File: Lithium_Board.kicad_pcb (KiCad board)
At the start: 6 copper layers, 80 x 67 mm, 117 parts, among them IC1 BQ25750RRVR, IC2 TPS70933DBVR, IC4 STM32G0B1CBT6N, IC5 TCAN3414DR, IC6 BQ7694204PFBR, J1 XT30PW-M, J2 XT30PW-F, J3 XT30PW-M, J4 S3B-XH-SM4-TB_LF__SN_, J5 TSW-105-07-G-S, J6 Conn_01x06, J7 Conn_01x04, Q1 SIR870ADP-T1-GE3, Q10 MMBT5551LT1G, Q2 SIR870ADP-T1-GE3, Q3 SIR870ADP-T1-GE3, Q4 SIR870ADP-T1-GE3, Q5 SIR870ADP-T1-GE3, Q6 SIR870ADP-T1-GE3, Q7 SIR870ADP-T1-GE3, Q8 SIR870ADP-T1-GE3

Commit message: Small Changes
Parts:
- added C29: 100nF [HV], C0603C104K1RACAUTO:CAPC1608X95N, B.Cu at (117.3, 74.2)
- added C30: 4.7uF [HV], KAM32LR72A475KU:CAPC3225X94N, B.Cu at (114.7, 74.0)
- moved R7 6.59 mm to (157.8, 89.1)
- moved C8 4.88 mm to (164.2, 81.1), turned to 0 degrees
- moved C23 0.88 mm to (174.2, 95.3)
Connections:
- net +48V renamed VIN
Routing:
- net +BATT: track 19.0 -> 7.41 mm, vias 29 -> 27
- net /Q1_D: track 0.00 -> 3.12 mm
- net /Q7_DRAIN: track 1.07 -> 3.84 mm, vias 46 -> 40
- net BQ_SYS: track 2.85 -> 5.42 mm
- net GND: track 65.5 -> 66.5 mm

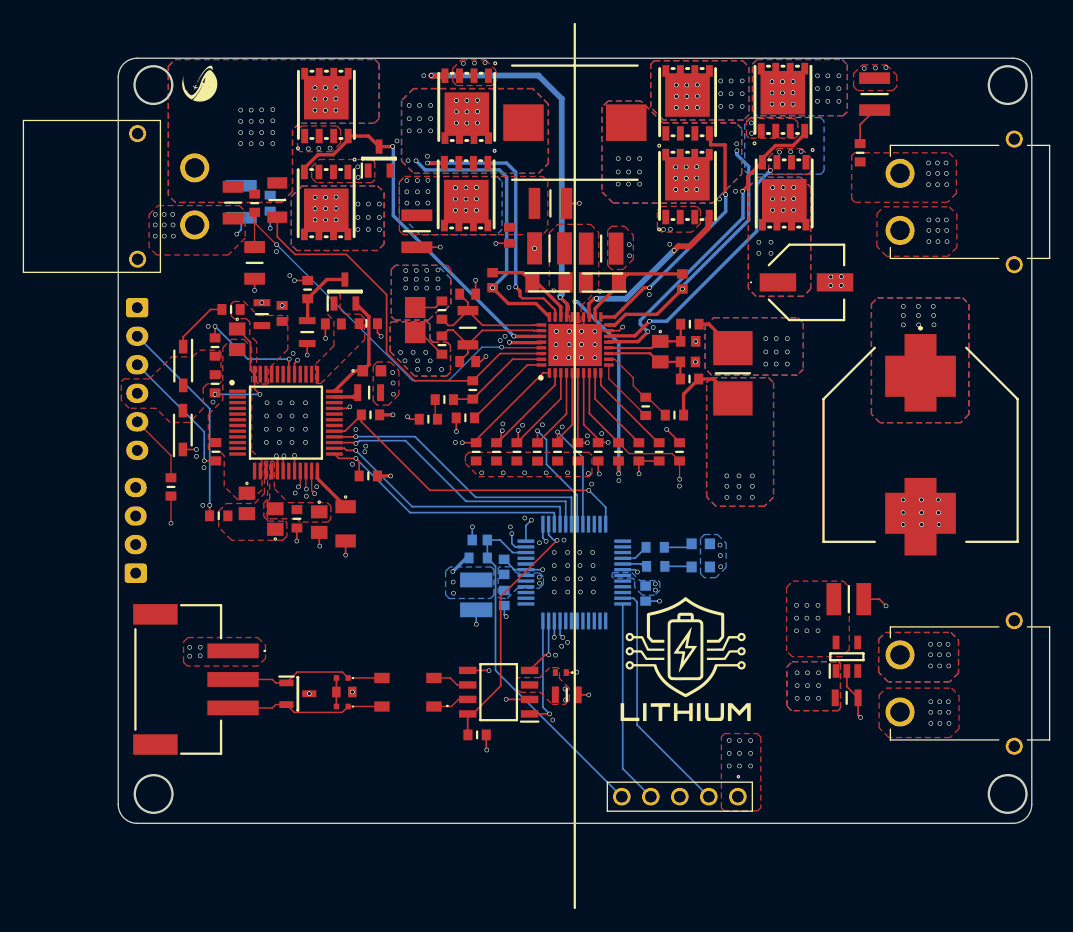
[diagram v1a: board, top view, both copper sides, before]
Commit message: Via Arrays Fixed
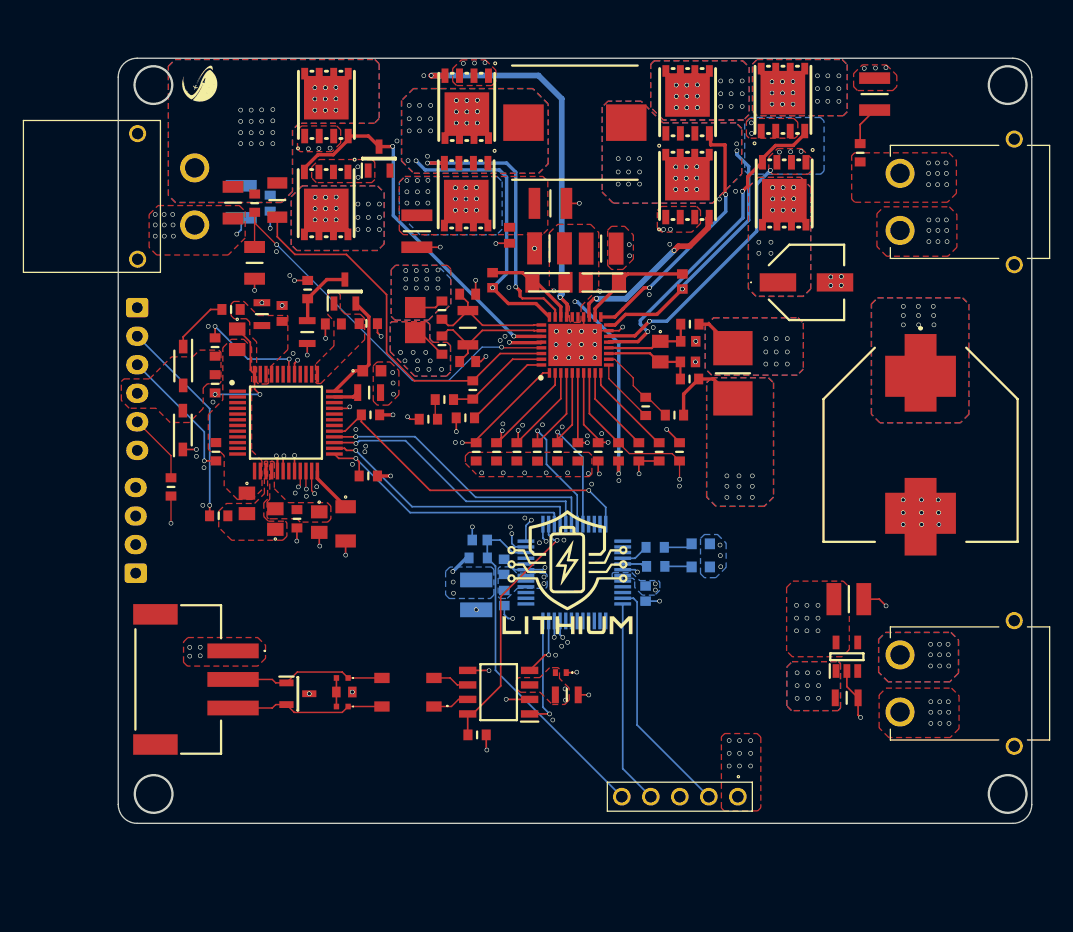
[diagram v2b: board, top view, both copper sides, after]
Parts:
- moved G*** 12.8 mm to (143.3, 106.8)
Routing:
- net GND: track 66.5 -> 66.2 mm, vias 198 -> 166

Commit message: Review Changes #2
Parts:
- moved G*** 1.68 mm to (176.3, 63.9)
- moved G*** 0.99 mm to (112.1, 63.7)
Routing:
- net /SW2: track 22.7 -> 23.5 mm
- net /HIDRV2: track 22.9 -> 22.3 mm
- net /ACDRV: track 33.3 -> 33.8 mm
- net GND: vias 166 -> 168
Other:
- outline, holes or cut-outs redrawn

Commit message: Vias in Pad Fixed
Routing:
- net BQ_SYS: vias 67 -> 76
- net /SW2: vias 20 -> 29
- net /SW1: vias 20 -> 29
- net /Q7_DRAIN: vias 40 -> 49

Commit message: First Big Review Changes
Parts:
- IC2: value TPS70933DBVR -> TPS70933DRVR; footprint TPS70933DBVR:SOT95P280X145-5N -> TPS70933DRVR:SON65P200X200X80-7N
- R11: value 249k -> 249kΩ; footprint RC0603FR-07249KL:RESC1608X55N -> RC0603FR-071KL:RESC1608X55N
- R25: value 34.8k -> 35.2kΩ; footprint RC0603FR-0734K8L:RESC1608X55N -> RC0603FR-071KL:RESC1608X55N
- moved C21 24.5 mm to (145.4, 126.1), turned to -90 degrees
- moved IC2 1.63 mm to (166.1, 113.9), turned to -90 degrees
- turned R11 to 0 degrees
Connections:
- IC2 pad 1: +BATT -> +3V3
- IC2 pad 2: GND -> unconnected-(IC2-NC_1-Pad2)
- IC2 pad 3: unconnected-(IC2-EN-Pad3) -> GND
- IC2 pad 5: +3V3 -> unconnected-(IC2-NC_2-Pad5)
- R11 pad 1: +BATT -> BQ_FB
- R11 pad 2: BQ_FB -> +BATT
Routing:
- net GND: track 66.2 -> 63.3 mm, vias 168 -> 173
- net NRST: track 31.2 -> 30.6 mm
- net +BATT: vias 27 -> 26

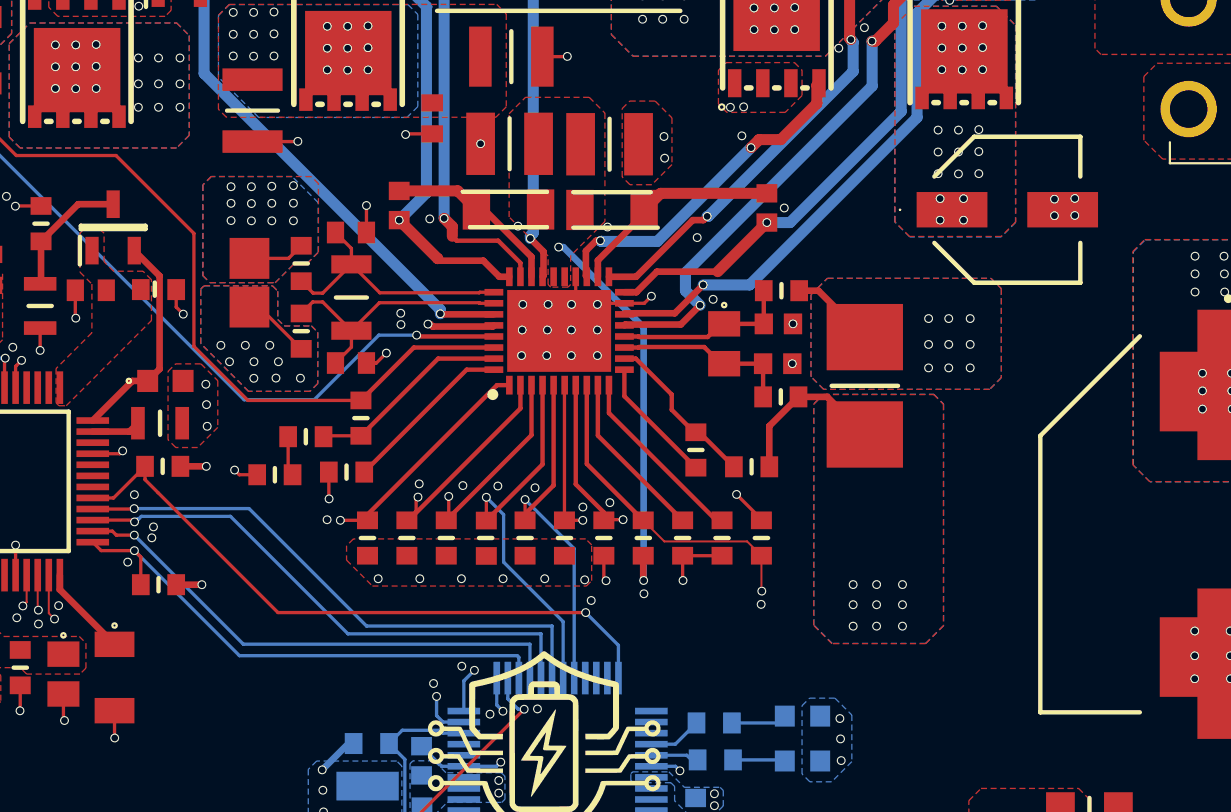
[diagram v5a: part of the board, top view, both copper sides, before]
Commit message: Fixed Big Capacitor
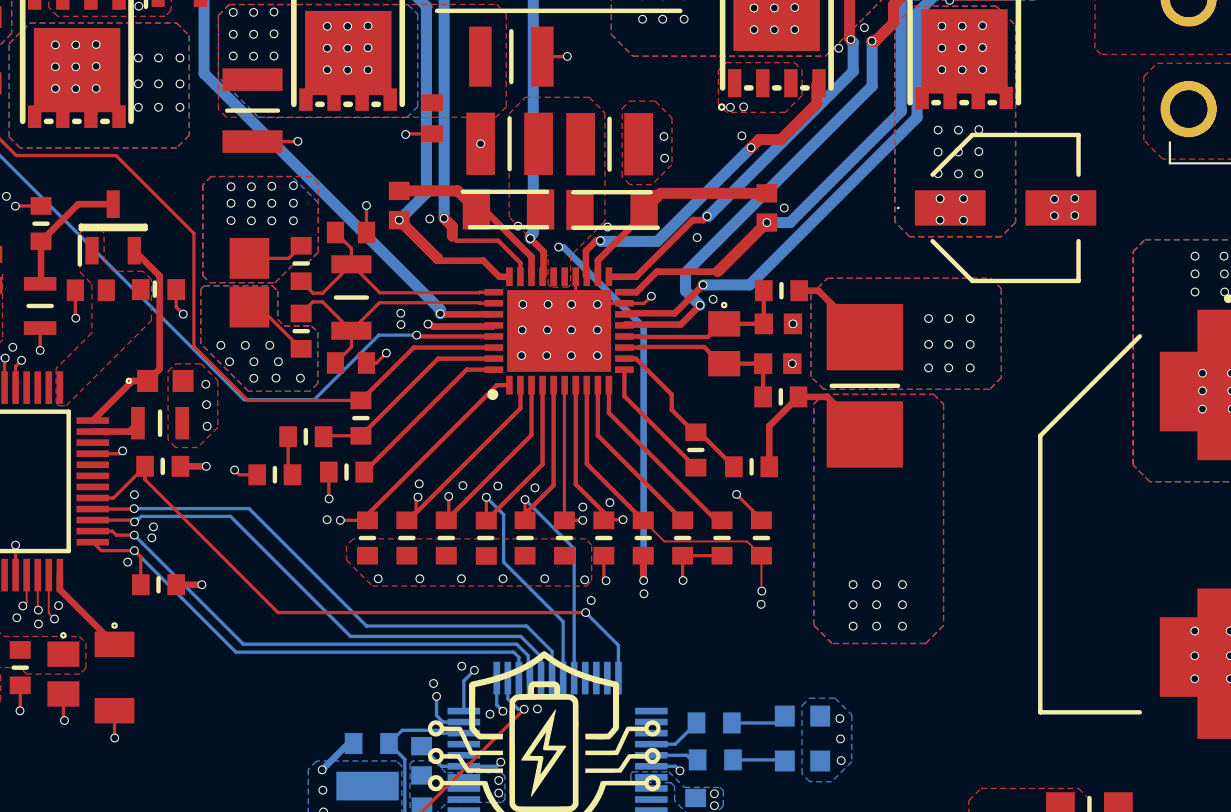
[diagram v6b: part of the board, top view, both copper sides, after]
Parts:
- C23: value EEV-FK2A101V -> EEE-TP1K391V; footprint EEV-FK2A101V:EEEFK0J682AV -> EEE-TP1K391V:EEEFK0J682AV
- moved C8 0.11 mm to (164.2, 81.0)
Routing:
- net BQ2_MOSI: track 25.3 -> 24.6 mm
- net BQ2_MISO: track 24.6 -> 24.0 mm
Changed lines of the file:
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@@
 	(footprint "EEE-FT1V101AP:EEE1AA101SP"
 		(layer "F.Cu")
-		(at 164.23 81.1)
+		(at 164.15 81.02)
 		(descr "SMD_Lytic_D")
 		(tags "Capacitor Polarised")
@@
 		)
 		(fp_line
-			(start -4.85 -4.025)
-			(end 4.1 -4.025)
+			(start -4.225 -3.55)
+			(end 4.175 -3.55)
 			(stroke
 				(width 0.05)
@@
 		)
 		(fp_line
-			(start -4.85 3.975)
-			(end -4.85 -4.025)
+			(start -4.225 3.6)
+			(end -4.225 -3.55)
 			(stroke
 				(width 0.05)
@@
 		)
 		(fp_line
-			(start 4.1 -4.025)
-			(end 4.1 3.975)
+			(start 4.175 -3.55)
+			(end 4.175 3.6)
 			(stroke
 				(width 0.05)
@@
 		)
 		(fp_line
-			(start 4.1 3.975)
-			(end -4.85 3.975)
+			(start 4.175 3.6)
+			(end -4.225 3.6)
 			(stroke
 				(width 0.05)
@@
 		)
 	)
-	(footprint "EEV-FK2A101V:EEEFK0J682AV"
+	(footprint "EEE-TP1K391V:EEEFK0J682AV"
 		(layer "F.Cu")
 		(at 174.22 95.32 180)
@@
 		(tags "Capacitor Polarised (6-Pin Vibration Proof)")
 		(property "Reference" "C23"
-			(at 8.71 -0.043333 90)
+			(at 10.55 0 90)
 			(layer "B.SilkS")
 			(effects
@@
 			)
 		)
-		(property "Value" "EEV-FK2A101V"
-			(at 0 0 0)
+		(property "Value" "EEE-TP1K391V"
+			(at 0 0 180)
 			(layer "F.SilkS")
 			(hide yes)
@@
 			)
 		)
-		(property "Datasheet" "http://industrial.panasonic.com/cdbs/www-data/pdf/RDE0000/ABA0000C1181.pdf"
-			(at 0 0 0)
+		(property "Datasheet" "http://industrial.panasonic.com/cdbs/www-data/pdf/RDE0000/RDE0000C1255.pdf"
+			(at 0 0 180)
 			(layer "F.Fab")
 			(hide yes)
@@
 			)
 		)
-		(property "Description" "Aluminium Electroyltic Capacitor, Radial, Vibration-Proof"
-			(at 0 0 0)
+		(property "Description" "Aluminum Electrolytic Capacitors - SMD 80VDC 390uF 20% SMD AEC-Q200 Vibe Proof"
+			(at 0 0 180)
 			(layer "F.Fab")
 			(hide yes)
@@
 			)
 		)
-		(property "Mouser Part Number" "667-EEV-FK2A101V"
+		(property "Mouser Part Number" "667-EEE-TP1K391V"
 			(at 0 0 180)
 			(unlocked yes)
@@
 			)
 		)
-		(property "Mouser Price/Stock" "https://www.mouser.co.uk/ProductDetail/Panasonic/EEV-FK2A101V?qs=MtOUKumLmnaVkoWQWMGNWA%3D%3D"
+		(property "Mouser Price/Stock" "https://www.mouser.co.uk/ProductDetail/Panasonic/EEE-TP1K391V?qs=XFmntM7Yc9dUeO1BN5vyvw%3D%3D"
 			(at 0 0 180)
 			(unlocked yes)
@@
 			)
 		)
-		(property "Manufacturer_Part_Number" "EEV-FK2A101V"
+		(property "Manufacturer_Part_Number" "EEE-TP1K391V"
 			(at 0 0 180)
 			(unlocked yes)
@@
 		)
 		(fp_line
-			(start 8.9 9.975)
-			(end 8.9 -10)
+			(start 8.925 10.575)
+			(end 8.925 -10)
 			(stroke
 				(width 0.1)
@@
 		)
 		(fp_line
-			(start 8.9 -10)
-			(end -8.975 -10)
+			(start 8.925 -10)
+			(end -8.825 -10)
 			(stroke
 				(width 0.1)
@@
 		)
 		(fp_line
-			(start -8.975 9.975)
-			(end 8.9 9.975)
+			(start -8.825 10.575)
+			(end 8.925 10.575)
 			(stroke
 				(width 0.1)
@@
 		)
 		(fp_line
-			(start -8.975 -10)
-			(end -8.975 9.975)
+			(start -8.825 -10)
+			(end -8.825 10.575)
 			(stroke
 				(width 0.1)
@@
 		)
 		(fp_text user "${REFERENCE}"
-			(at 8.71 -0.043333 90)
+			(at 10.55 0 90)
 			(layer "B.Fab")
 			(effects
@@
 		)
 		(embedded_fonts no)
-		(model "${KIPRJMOD}/Lithium_Footprints/LIB_EEV-FK2A101V/EEV-FK2A101V/3D/EEV-FK2A101V.stp"
+		(model "EEE-TP1K391V.stp"
 			(offset
 				(xyz 0 0 0)
@@
 			)
 			(rotate
-				(xyz 90 180 90)
+				(xyz -90 0 -90)
 			)
 		)
@@
 	)
 	(segment
-		(start 142.076 101.258499)
-		(end 142.15 101.332499)
+		(start 129.36 101.1)
+		(end 141.917501 101.1)
 		(width 0.15)
 		(layer "B.Cu")
@@
 	)
 	(segment
-		(start 124.77 96.51)
-		(end 129.518499 101.258499)
+		(start 142.15 101.332499)
+		(end 142.15 102.271999)
 		(width 0.15)
 		(layer "B.Cu")
@@
 	)
 	(segment
-		(start 142.15 101.332499)
-		(end 142.15 102.271999)
+		(start 124.77 96.51)
+		(end 129.36 101.1)
 		(width 0.15)
 		(layer "B.Cu")
@@
 	)
 	(segment
-		(start 129.518499 101.258499)
-		(end 142.076 101.258499)
+		(start 141.917501 101.1)
+		(end 142.15 101.332499)
 		(width 0.15)
 		(layer "B.Cu")
@@
 	)
 	(segment
-		(start 124.765489 95.809614)
-		(end 129.695875 100.74)
+		(start 142.053889 100.74)
+		(end 142.576 101.262111)
 		(width 0.15)
 		(layer "B.Cu")
@@
 	)
 	(segment
-		(start 142.65 100.74)
+		(start 142.576 102.197999)
 		(end 142.65 102.271999)
 		(width 0.15)
@@
 	(segment
 		(start 129.695875 100.74)
-		(end 142.65 100.74)
+		(end 142.053889 100.74)
+		(width 0.15)
+		(layer "B.Cu")
+		(net 56)
+	)
+	(segment
+		(start 142.576 101.262111)
+		(end 142.576 102.197999)
+		(width 0.15)
+		(layer "B.Cu")
+		(net 56)
+	)
+	(segment
+		(start 124.765489 95.809614)
+		(end 129.695875 100.74)
 		(width 0.15)
 		(layer "B.Cu")
@@
 	)
 	(segment
-		(start 135.263166 99.92)
-		(end 143.65 99.92)
+		(start 143.65 101.07)
+		(end 143.65 102.271999)
 		(width 0.15)
 		(layer "B.Cu")
@@
 	)
 	(segment
-		(start 143.65 99.92)
-		(end 143.65 102.271999)
+		(start 142.5 99.92)
+		(end 143.65 101.07)
+		(width 0.15)
+		(layer "B.Cu")
+		(net 98)
+	)
+	(segment
+		(start 135.263166 99.92)
+		(end 142.5 99.92)
 		(width 0.15)
 		(layer "B.Cu")
@@
 	)
 	(segment
-		(start 134.424746 100.271)
-		(end 143.15 100.271)
+		(start 124.777811 95.209738)
+		(end 124.901549 95.086)
+		(width 0.15)
+		(layer "B.Cu")
+		(net 128)
+	)
+	(segment
+		(start 125.082166 94.961)
+		(end 129.114746 94.961)
 		(width 0.15)
 		(layer "B.Cu")
@@
 	)
 	(segment
-		(start 129.114746 94.961)
-		(end 134.424746 100.271)
+		(start 134.542746 100.389)
+		(end 142.239 100.389)
 		(width 0.15)
 		(layer "B.Cu")
@@
 	)
 	(segment
-		(start 124.777811 95.209738)
-		(end 124.901549 95.086)
+		(start 142.239 100.389)
+		(end 143.15 101.3)
 		(width 0.15)
 		(layer "B.Cu")
@@
 	)
 	(segment
-		(start 143.15 100.271)
+		(start 143.15 101.3)
 		(end 143.15 102.271999)
 		(width 0.15)
@@
 	)
 	(segment
-		(start 124.957166 95.086)
-		(end 125.082166 94.961)
+		(start 129.114746 94.961)
+		(end 134.542746 100.389)
 		(width 0.15)
 		(layer "B.Cu")
@@
 	)
 	(segment
-		(start 125.082166 94.961)
-		(end 129.114746 94.961)
+		(start 124.957166 95.086)
+		(end 125.082166 94.961)
 		(width 0.15)
 		(layer "B.Cu")
